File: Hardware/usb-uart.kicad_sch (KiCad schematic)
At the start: 9 parts, among them J2 USB_C_Receptacle_USB2.0

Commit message: schematic done? + footprints assigned
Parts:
- J2: footprint Connector_USB:USB_C_Receptacle_GCT_USB4085 -> Connector_USB:USB_C_Receptacle_Palconn_UTC16-G
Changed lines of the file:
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@@
       (effects (font (size 1.27 1.27)))
     )
-    (property "Footprint" "Connector_USB:USB_C_Receptacle_GCT_USB4085" (at 104.14 104.14 0)
+    (property "Footprint" "Connector_USB:USB_C_Receptacle_Palconn_UTC16-G" (at 104.14 104.14 0)
       (effects (font (size 1.27 1.27)) hide)
     )

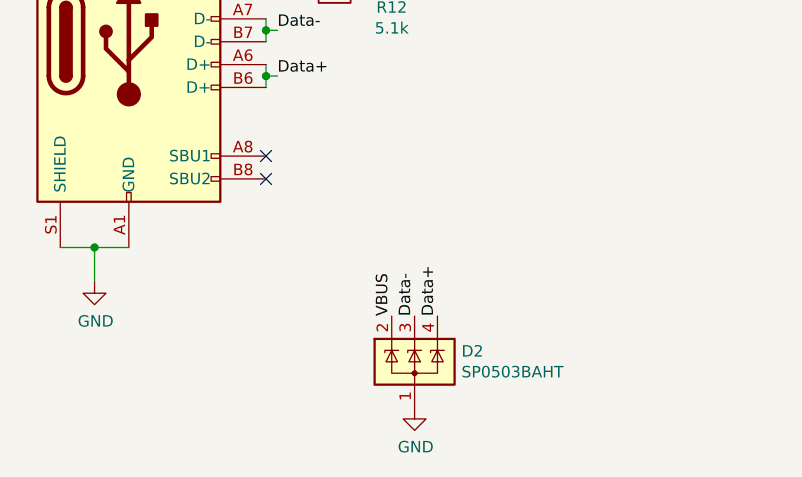
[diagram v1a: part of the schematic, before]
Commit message: high V side finished, CAN circuit and ESP left to place
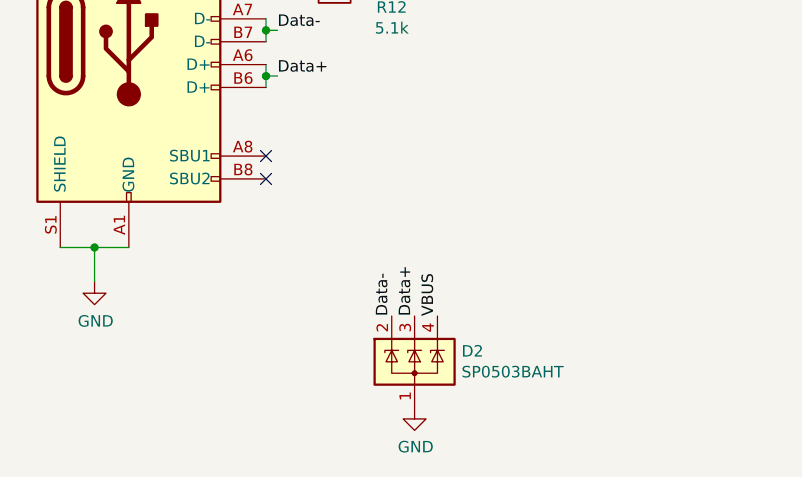
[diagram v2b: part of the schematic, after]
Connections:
- net Data+: now also D2.3 (K); no longer D2.4 (K)
- net Data-: now also D2.2 (K); no longer D2.3 (K)
- net VBUS: now also D2.4 (K); no longer D2.2 (K)
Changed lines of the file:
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@@
     (stroke (width 0) (type default))
   )
-  (label "Data+" (at 134.62 134.62 90) (fields_autoplaced)
+  (label "Data-" (at 129.54 134.62 90) (fields_autoplaced)
     (effects (font (size 1.27 1.27)) (justify left bottom))
   )
-  (label "VBUS" (at 129.54 134.62 90) (fields_autoplaced)
+  (label "VBUS" (at 134.62 134.62 90) (fields_autoplaced)
     (effects (font (size 1.27 1.27)) (justify left bottom))
   )
@@
   )
   (label "Data-" (at 44.45 99.06 0) (fields_autoplaced)
-    (effects (font (size 1.27 1.27)) (justify left bottom))
-  )
-  (label "Data-" (at 132.08 134.62 90) (fields_autoplaced)
     (effects (font (size 1.27 1.27)) (justify left bottom))
   )
@@
     (effects (font (size 1.27 1.27)) (justify left bottom))
   )
+  (label "Data+" (at 132.08 134.62 90) (fields_autoplaced)
+    (effects (font (size 1.27 1.27)) (justify left bottom))
+  )

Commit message: finished? (pre-review)
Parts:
- removed TP3: TestPoint, TestPoint:TestPoint_Pad_D1.0mm, symbol Connector:TestPoint
- USBLED1: footprint Resistor_SMD:R_0402_1005Metric -> Diode_SMD:D_0402_1005Metric
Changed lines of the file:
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@@
-    (stroke (width 0) (type default))
-  )
-  (wire (pts (xy 44.45 109.22) (xy 52.07 109.22))
     (stroke (width 0) (type default))
   )
@@
   )
   (label "Data-" (at 116.84 102.87 0) (fields_autoplaced)
-    (effects (font (size 1.27 1.27)) (justify left bottom))
-  )
-  (label "VBUS" (at 44.45 109.22 0) (fields_autoplaced)
     (effects (font (size 1.27 1.27)) (justify left bottom))
   )
@@
     )
   )
-  (symbol (lib_id "Connector:TestPoint") (at 52.07 109.22 270) (unit 1)
-    (in_bom yes) (on_board yes) (dnp no)
-    (property "Reference" "TP3" (at 56.8452 108.0516 90)
-      (effects (font (size 1.27 1.27)) (justify left))
-    )
-    (property "Value" "TestPoint" (at 56.8452 110.363 90)
-      (effects (font (size 1.27 1.27)) (justify left))
-    )
-    (property "Footprint" "TestPoint:TestPoint_Pad_D1.0mm" (at 52.07 114.3 0)
-      (effects (font (size 1.27 1.27)) hide)
-    )
-    (property "Datasheet" "~" (at 52.07 114.3 0)
-      (effects (font (size 1.27 1.27)) hide)
-    )
-    (pin "1")
-    (instances
-      (project "flintandsteel"
-        (path "/7db990e4-92e1-4f99-b4d2-435bbec1ba83/00000000-0000-0000-0000-000061925999"
-          (reference "TP3") (unit 1)
-        )
-      )
-    )
-  )
   (symbol (lib_id "Device:LED_Small") (at 162.56 92.71 180) (unit 1)
     (in_bom yes) (on_board yes) (dnp no)
@@
       (effects (font (size 1.27 1.27)))
     )
-    (property "Footprint" "Resistor_SMD:R_0402_1005Metric" (at 162.56 92.71 90)
-      (effects (font (size 1.27 1.27)) hide)
-    )
+    (property "Footprint" "Diode_SMD:D_0402_1005Metric" (at 162.56 92.71 90)
+      (effects (font (size 1.27 1.27)) hide)
+    )

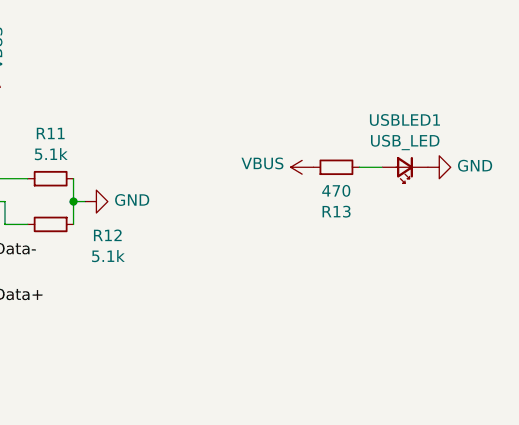
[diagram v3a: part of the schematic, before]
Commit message: mostly finished new power layout, needs some vias and i2c routing
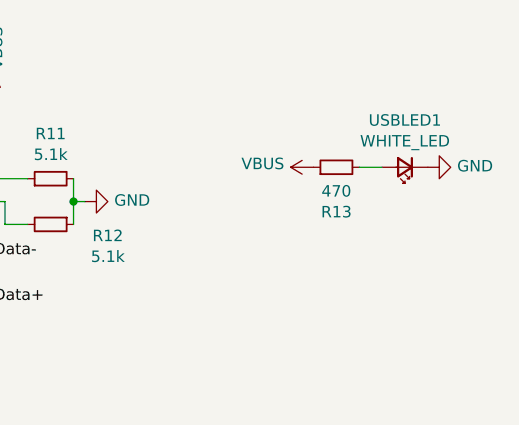
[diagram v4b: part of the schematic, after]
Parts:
- USBLED1: value USB_LED -> WHITE_LED
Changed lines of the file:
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@@
       (effects (font (size 1.27 1.27)))
     )
-    (property "Value" "USB_LED" (at 162.56 89.8144 0)
+    (property "Value" "WHITE_LED" (at 162.56 89.8144 0)
       (effects (font (size 1.27 1.27)))
     )

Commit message: v2.1 ordering
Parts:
- R13: value 470 -> 5.1k
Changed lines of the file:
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@@
       (effects (font (size 1.27 1.27)))
     )
-    (property "Value" "470" (at 154.94 95.377 90)
+    (property "Value" "5.1k" (at 154.94 95.377 90)
       (effects (font (size 1.27 1.27)))
     )
